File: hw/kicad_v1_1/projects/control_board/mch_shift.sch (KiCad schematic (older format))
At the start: 4 parts, among them U3 74HC595, U4 74HC595

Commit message: Update
Begin work on updating for rev1.1.
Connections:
- net labels added: +5V, N0_A, N0_B, N0_C, N0_D, N1_A, N1_B, N1_C, N1_D, N2_A, N2_B, N2_C, N2_D, N3_A, N3_B, N3_C, N3_D, SEL_N0_A, SEL_N0_B, SEL_N0_C, SEL_N0_D, SEL_N1_A, SEL_N1_B, SEL_N1_C, SEL_N1_D, SEL_N2_A, SEL_N2_B, SEL_N2_C, SEL_N2_D, SEL_N3_A, SEL_N3_B, SEL_N3_C, SEL_N3_D
- net labels removed: +3.3V, D0, D1, S0, S1, S2, S3, S4, S5, S6, S7, S8, S9, SEL_DOT_BOT, SEL_DOT_TOP, SEL_EIGHT, SEL_FIVE, SEL_FOUR, SEL_NINE, SEL_NIX0, SEL_NIX1, SEL_NIX2, SEL_NIX3, SEL_ONE, SEL_SEVEN, SEL_SIX, SEL_THREE, SEL_TWO, SEL_ZERO, SN0, SN1, SN2, SN3, TUBE_SEL
- wire segments 70 -> 76

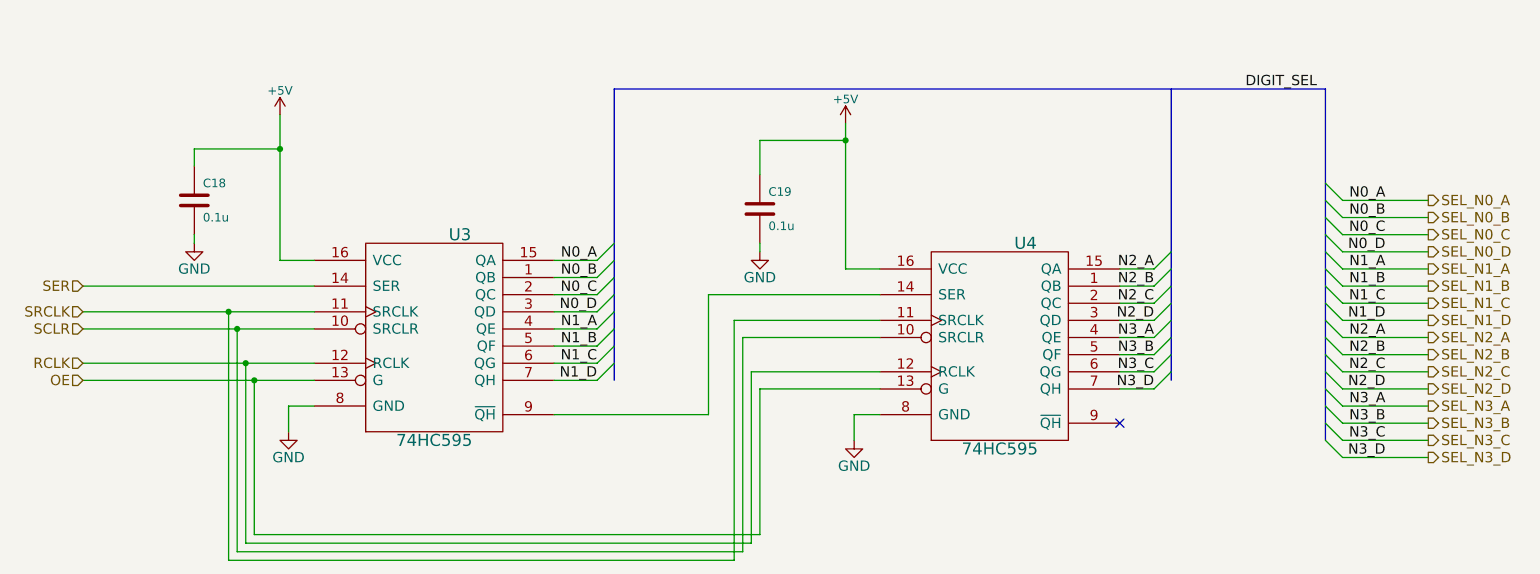
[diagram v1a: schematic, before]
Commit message: Schematic Work Complete
Check in schematic work before touching PCB. This should give me a point
to go back to if it all goes to hell.
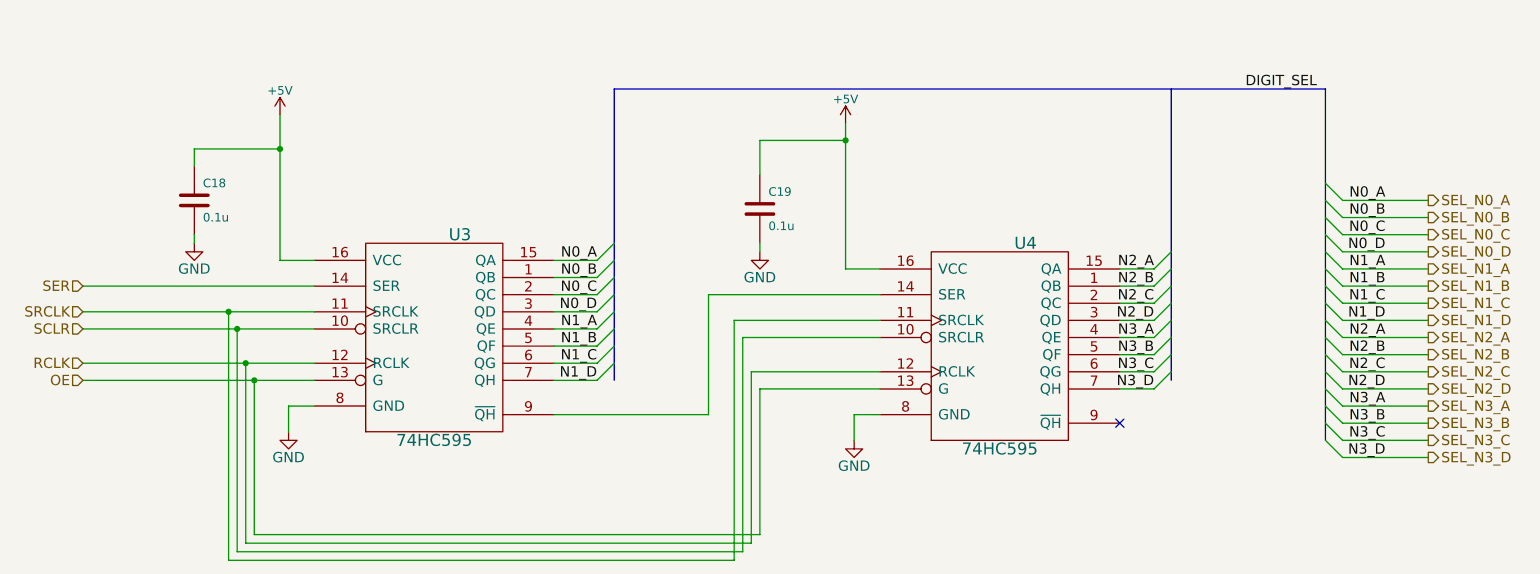
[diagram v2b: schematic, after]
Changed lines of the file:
@@
 $Descr A4 11693 8268
 encoding utf-8
-Sheet 5 6
+Sheet 6 6
 Title "Control Board"
 Date "2016-09-14"
@@
 	3550 3150 3750 3150
 Wire Wire Line
-	3550 2300 3550 2500
-Wire Wire Line
-	3550 2500 3550 3150
+	3550 2300 3550 3150
 Wire Bus Line
-	9650 2150 9650 2700
-Wire Bus Line
-	9650 2700 9650 2800
-Wire Bus Line
-	9650 2800 9650 2900
-Wire Bus Line
-	9650 2900 9650 3000
-Wire Bus Line
-	9650 3000 9650 3100
-Wire Bus Line
-	9650 3100 9650 3200
-Wire Bus Line
-	9650 3200 9650 3300
-Wire Bus Line
-	9650 3300 9650 3400
-Wire Bus Line
-	9650 3400 9650 3500
-Wire Bus Line
-	9650 3500 9650 3600
-Wire Bus Line
-	9650 3600 9650 3700
-Wire Bus Line
-	9650 3700 9650 3800
-Wire Bus Line
-	9650 3800 9650 3900
-Wire Bus Line
-	9650 3900 9650 4000
-Wire Bus Line
-	9650 4000 9650 4100
-Wire Bus Line
-	9650 4100 9650 4200
+	9650 2150 9650 4200
 Wire Wire Line
 	9750 2800 10250 2800
@@
 	6050 3350 7050 3350
 Wire Wire Line
-	2400 3450 3250 3450
-Wire Wire Line
-	3250 3450 3750 3450
+	2400 3450 3750 3450
 Wire Wire Line
 	3250 3450 3250 4900
@@
 	6200 3500 7050 3500
 Wire Wire Line
-	2400 3550 3300 3550
-Wire Wire Line
-	3300 3550 3750 3550
+	2400 3550 3750 3550
 Wire Wire Line
 	3300 3550 3300 4850
@@
 	6250 3600 7050 3600
 Wire Wire Line
-	2400 3750 3350 3750
-Wire Wire Line
-	3350 3750 3750 3750
+	2400 3750 3750 3750
 Wire Wire Line
 	3350 3750 3350 4800
@@
 	6300 3800 7050 3800
 Wire Wire Line
-	2400 3850 3400 3850
-Wire Wire Line
-	3400 3850 3750 3850
+	2400 3850 3750 3850
 Wire Wire Line
 	3400 3850 3400 4750
@@
 Connection ~ 3400 3850
 Wire Bus Line
-	5500 2150 5500 3050
-Wire Bus Line
-	5500 3050 5500 3150
-Wire Bus Line
-	5500 3150 5500 3250
-Wire Bus Line
-	5500 3250 5500 3350
-Wire Bus Line
-	5500 3350 5500 3450
-Wire Bus Line
-	5500 3450 5500 3550
-Wire Bus Line
-	5500 3550 5500 3650
-Wire Bus Line
-	5500 3650 5500 3750
-Wire Bus Line
-	5500 3750 5500 3850
+	5500 2150 5500 3850
 Wire Bus Line
 	5500 2150 9650 2150
 Wire Bus Line
-	8750 2150 8750 3100
-Wire Bus Line
-	8750 3100 8750 3200
-Wire Bus Line
-	8750 3200 8750 3300
-Wire Bus Line
-	8750 3300 8750 3400
-Wire Bus Line
-	8750 3400 8750 3500
-Wire Bus Line
-	8750 3500 8750 3600
-Wire Bus Line
-	8750 3600 8750 3700
-Wire Bus Line
-	8750 3700 8750 3800
-Wire Bus Line
-	8750 3800 8750 3850
+	8750 2150 8750 3850
 Wire Wire Line
 	5150 3850 5400 3850
@@
 	6350 2450 6850 2450
 Wire Wire Line
-	6850 2350 6850 2450
-Wire Wire Line
-	6850 2450 6850 3200
+	6850 2350 6850 3200
 Wire Wire Line
 	6850 3200 7050 3200

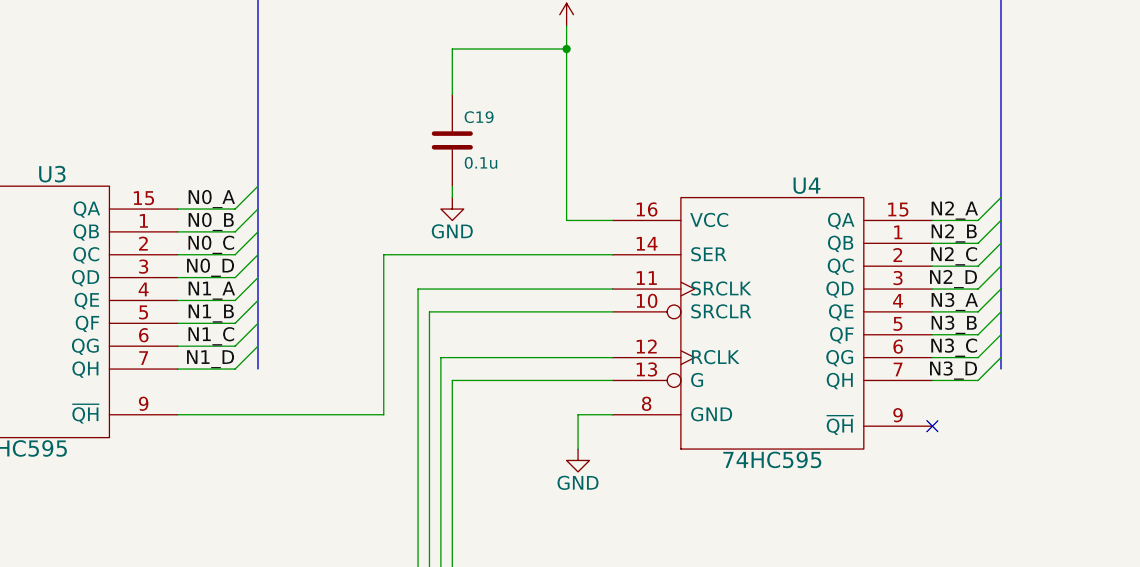
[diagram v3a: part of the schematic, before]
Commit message: Complete with errors
Check in before moving header. Currently the headers don't match up. If
I'm going to connect them with standard header I need to move it
significantly. Check in as a roll back point.
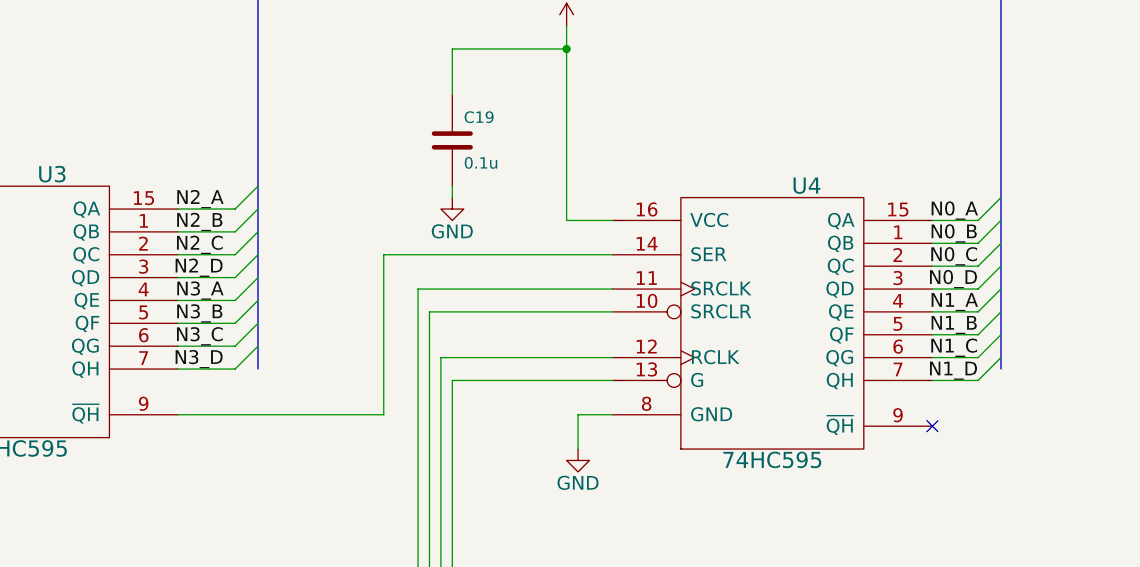
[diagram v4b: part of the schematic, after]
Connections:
- net SEL_N0_A: now also U4.15 (QA); no longer U3.15 (QA)
- net SEL_N0_B: now also U4.1 (QB); no longer U3.1 (QB)
- net SEL_N0_C: now also U4.2 (QC); no longer U3.2 (QC)
- net SEL_N0_D: now also U4.3 (QD); no longer U3.3 (QD)
- net SEL_N1_A: now also U4.4 (QE); no longer U3.4 (QE)
- net SEL_N1_B: now also U4.5 (QF); no longer U3.5 (QF)
- net SEL_N1_C: now also U4.6 (QG); no longer U3.6 (QG)
- net SEL_N1_D: now also U4.7 (QH); no longer U3.7 (QH)
- net SEL_N2_A: now also U3.15 (QA); no longer U4.15 (QA)
- net SEL_N2_B: now also U3.1 (QB); no longer U4.1 (QB)
- net SEL_N2_C: now also U3.2 (QC); no longer U4.2 (QC)
- net SEL_N2_D: now also U3.3 (QD); no longer U4.3 (QD)
- net SEL_N3_A: now also U3.4 (QE); no longer U4.4 (QE)
- net SEL_N3_B: now also U3.5 (QF); no longer U4.5 (QF)
- net SEL_N3_C: now also U3.6 (QG); no longer U4.6 (QG)
- net SEL_N3_D: now also U3.7 (QH); no longer U4.7 (QH)
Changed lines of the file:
@@
 RCLK
 $Comp
-L GND #PWR050
+L GND #PWR051
 U 1 1 54DAEE96
 P 6900 4200
-F 0 "#PWR050" H 6900 3950 60  0001 C CNN
+F 0 "#PWR051" H 6900 3950 60  0001 C CNN
 F 1 "GND" H 6900 4050 60  0000 C CNN
 F 2 "" H 6900 4200 60  0000 C CNN
@@
 $EndComp
 $Comp
-L GND #PWR051
+L GND #PWR052
 U 1 1 54DAEEAC
 P 3600 4150
-F 0 "#PWR051" H 3600 3900 60  0001 C CNN
+F 0 "#PWR052" H 3600 3900 60  0001 C CNN
 F 1 "GND" H 3600 4000 60  0000 C CNN
 F 2 "" H 3600 4150 60  0000 C CNN
@@
 Entry Wire Line
 	8750 3100 8650 3200
-Text Label 5400 3150 2    60   ~ 0
+Text Label 8650 3200 2    60   ~ 0
 N0_A
-Text Label 5400 3250 2    60   ~ 0
+Text Label 8650 3300 2    60   ~ 0
 N0_B
-Text Label 5400 3350 2    60   ~ 0
+Text Label 8650 3400 2    60   ~ 0
 N0_C
-Text Label 5400 3450 2    60   ~ 0
+Text Label 8650 3500 2    60   ~ 0
 N0_D
-Text Label 5400 3550 2    60   ~ 0
+Text Label 8650 3600 2    60   ~ 0
 N1_A
-Text Label 5400 3650 2    60   ~ 0
+Text Label 8650 3700 2    60   ~ 0
 N1_B
-Text Label 5400 3750 2    60   ~ 0
+Text Label 8650 3800 2    60   ~ 0
 N1_C
-Text Label 5400 3850 2    60   ~ 0
+Text Label 8650 3900 2    60   ~ 0
 N1_D
-Text Label 8650 3200 2    60   ~ 0
+Text Label 5350 3150 2    60   ~ 0
 N2_A
-Text Label 8650 3300 2    60   ~ 0
+Text Label 5350 3250 2    60   ~ 0
 N2_B
 Text HLabel 10250 3800 2    60   Output ~ 0
@@
 Entry Wire Line
 	8750 3300 8650 3400
-Text Label 8650 3400 2    60   ~ 0
+Text Label 5350 3350 2    60   ~ 0
 N2_C
-Text Label 8650 3500 2    60   ~ 0
+Text Label 5350 3450 2    60   ~ 0
 N2_D
 $Comp
-L GND #PWR052
+L GND #PWR053
 U 1 1 54DB0426
 P 3050 3050
-F 0 "#PWR052" H 3050 2800 60  0001 C CNN
+F 0 "#PWR053" H 3050 2800 60  0001 C CNN
 F 1 "GND" H 3050 2900 60  0000 C CNN
 F 2 "" H 3050 3050 60  0000 C CNN
@@
 $EndComp
 $Comp
-L GND #PWR053
+L GND #PWR054
 U 1 1 54DB062A
 P 6350 3100
-F 0 "#PWR053" H 6350 2850 60  0001 C CNN
+F 0 "#PWR054" H 6350 2850 60  0001 C CNN
 F 1 "GND" H 6350 2950 60  0000 C CNN
 F 2 "" H 6350 3100 60  0000 C CNN
@@
 Wire Wire Line
 	8450 3900 8650 3900
-Text Label 8650 3600 2    60   ~ 0
+Text Label 5350 3550 2    60   ~ 0
 N3_A
-Text Label 8650 3700 2    60   ~ 0
+Text Label 5350 3650 2    60   ~ 0
 N3_B
-Text Label 8650 3800 2    60   ~ 0
+Text Label 5350 3750 2    60   ~ 0
 N3_C
-Text Label 8650 3900 2    60   ~ 0
+Text Label 5350 3850 2    60   ~ 0
 N3_D
 Text Label 10000 3600 2    60   ~ 0
@@
 	9750 4300 10250 4300
 $Comp
-L +5V #PWR054
+L +5V #PWR055
 U 1 1 581F3103
 P 6850 2350
-F 0 "#PWR054" H 6850 2200 50  0001 C CNN
+F 0 "#PWR055" H 6850 2200 50  0001 C CNN
 F 1 "+5V" H 6850 2490 50  0000 C CNN
 F 2 "" H 6850 2350 50  0000 C CNN
@@
 $EndComp
 $Comp
-L +5V #PWR055
+L +5V #PWR056
 U 1 1 581F311F
 P 3550 2300
-F 0 "#PWR055" H 3550 2150 50  0001 C CNN
+F 0 "#PWR056" H 3550 2150 50  0001 C CNN
 F 1 "+5V" H 3550 2440 50  0000 C CNN
 F 2 "" H 3550 2300 50  0000 C CNN
